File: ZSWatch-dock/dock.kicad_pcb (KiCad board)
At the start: 2 copper layers, 55.1 x 32.5 mm, 22 parts, among them IC1 STM32F072CBT6, IC2 TCR3UF20A,LM_CT, IC3 TXB0104QPWRQ1, IC4 XC9265C181MR-G, J1 USB4105-GF-A, J2 8.06.16, J3 Charger and programming heade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

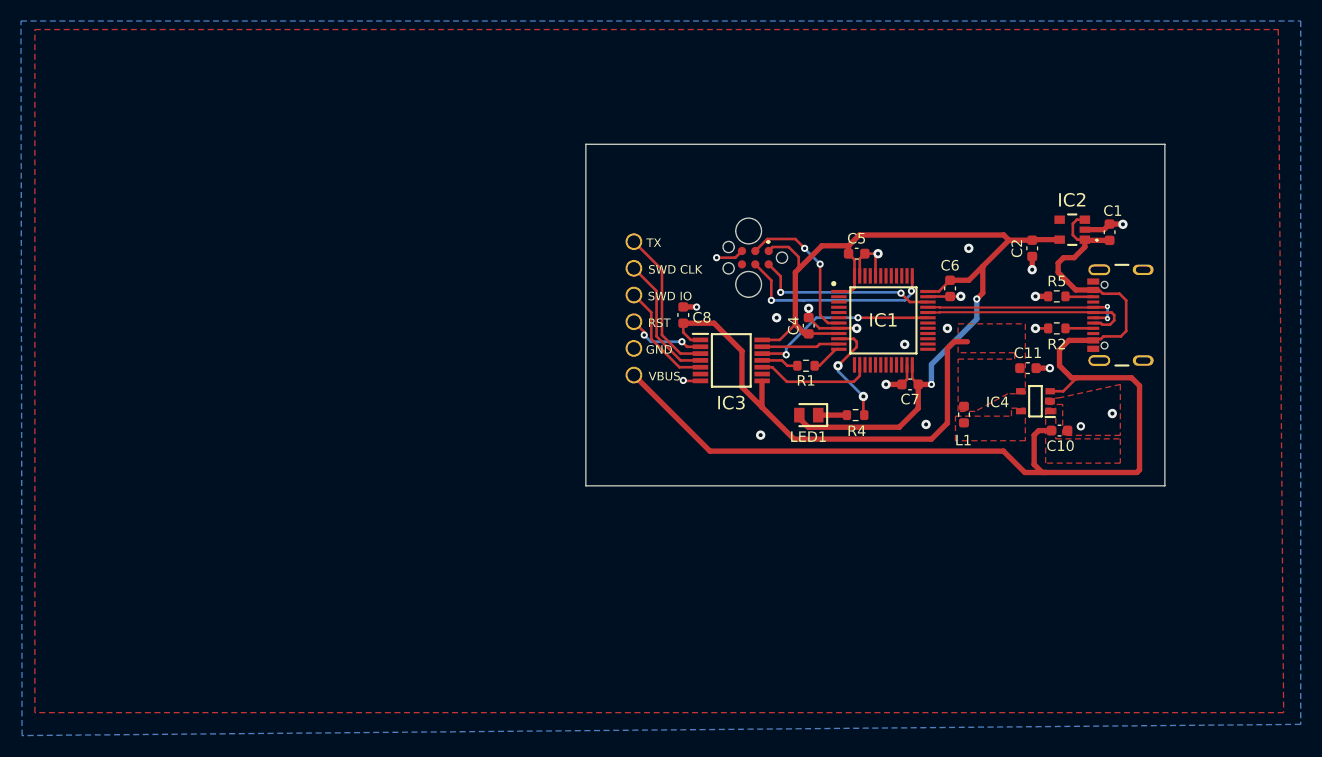
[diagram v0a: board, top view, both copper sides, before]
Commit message: Finished dock/debugger/programmer PCB.
Moved connectors around.
Added missing silkscreen.
Added extra connector for easy access to pins such as power etc.
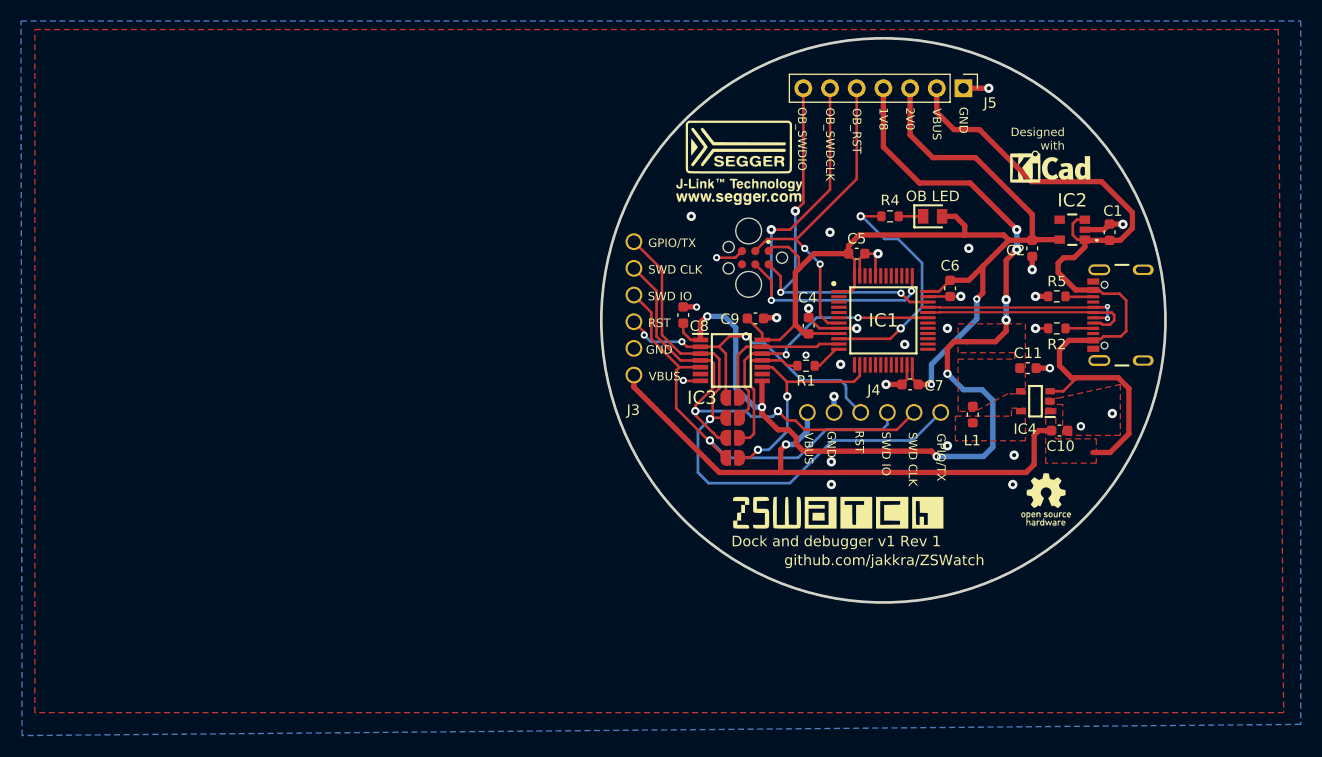
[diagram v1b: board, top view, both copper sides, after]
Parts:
- added C9: 0.1uF, Capacitor_SMD:C_0603_1608Metric, F.Cu at (140.7, 76.8)
- added G***: LOGO, LOGO, F.Cu at (168.9, 62.2)
- added G***: LOGO, LOGO, F.Cu at (148.6, 95.2)
- added G***: LOGO, LOGO, F.Cu at (168.4, 94.0)
- added G***: LOGO, LOGO, F.Cu at (139.2, 62.0)
- added J4: Charger and programming header (Placeholder), user_library:rtlecs-6-pin-2-54, F.Cu at (152.0, 85.7)
- added J5: Conn_01x07, Connector_PinHeader_2.54mm:PinHeader_1x07_P2.54mm_Vertical, F.Cu at (160.5, 54.9)
- added JP1: SolderJumper_2_Open, Jumper:SolderJumper-2_P1.3mm_Open_RoundedPad1.0x1.5mm, F.Cu at (138.6, 84.3)
- added JP2: SolderJumper_2_Open, Jumper:SolderJumper-2_P1.3mm_Open_RoundedPad1.0x1.5mm, F.Cu at (138.6, 88.1)
- added JP3: SolderJumper_2_Open, Jumper:SolderJumper-2_P1.3mm_Open_RoundedPad1.0x1.5mm, F.Cu at (138.6, 90.0)
- added JP4: SolderJumper_2_Open, Jumper:SolderJumper-2_P1.3mm_Open_RoundedPad1.0x1.5mm, F.Cu at (138.6, 86.2)
- OB LED: renamed from LED1
- moved OB LED 22.3 mm to (157.6, 67.1), turned to 0 degrees
- moved R4 19.2 mm to (153.5, 67.1), turned to 180 degrees
- moved L1 0.84 mm to (161.4, 85.9)
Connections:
- net Net-(IC3-Pad11) renamed /ZSWATCH_H_SWDCLK_PRE
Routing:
- net +1V8: track 46.9 -> 95.1 mm, vias 0 -> 8
- net /ZSWATCH_L_TX: track 14.4 -> 55.9 mm, vias 0 -> 1
- net /ZSWATCH_L_SWDCLK: track 12.5 -> 46.0 mm, vias 0 -> 2
- net /ZSWATCH_L_SWDIO: track 10.7 -> 41.5 mm, vias 0 -> 1
- net VBUS: track 107.6 -> 132.8 mm, vias 0 -> 1
- net /ZSWATCH_L_RESET: track 7.49 -> 31.9 mm, vias 2 -> 3
- net /OB_CLK: track 19.4 -> 42.9 mm, vias 2 -> 3
- net /OB_SWDIO: track 17.5 -> 37.9 mm, vias 2 -> 3
- net /OB_RESET: track 14.6 -> 31.5 mm
- net LED_OB: track 10.6 -> 23.0 mm
- net +2V0: track 91.9 -> 104.3 mm
- net /ZSWATCH_H_SWDIO: track 11.1 -> 21.5 mm, vias 0 -> 2
- net /ZSWATCH_H_SWDCLK_PRE: track 3.56 -> 13.2 mm
- net ZSWATCH_H_TX: track 17.7 -> 25.6 mm
- net /ZSWATCH_H_RESET: track 7.41 -> 14.2 mm
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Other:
- board size 55.1 x 32.5 mm -> 53.7 x 53.7 mm
- board text added: "1V8"
- board text added: "2V0"
- board text added: "Designed with"
- board text added: "Dock and debugger v1 Rev 1"
- board text added: "GPIO"
- board text added: "GPIO/TX"
- board text added: "OB_RST"
- board text added: "OB_SWDCLK"
- board text added: "OB_SWDIO"
- board text added: "github.com/jakkra/ZSWatch"
- board text removed: "TX"

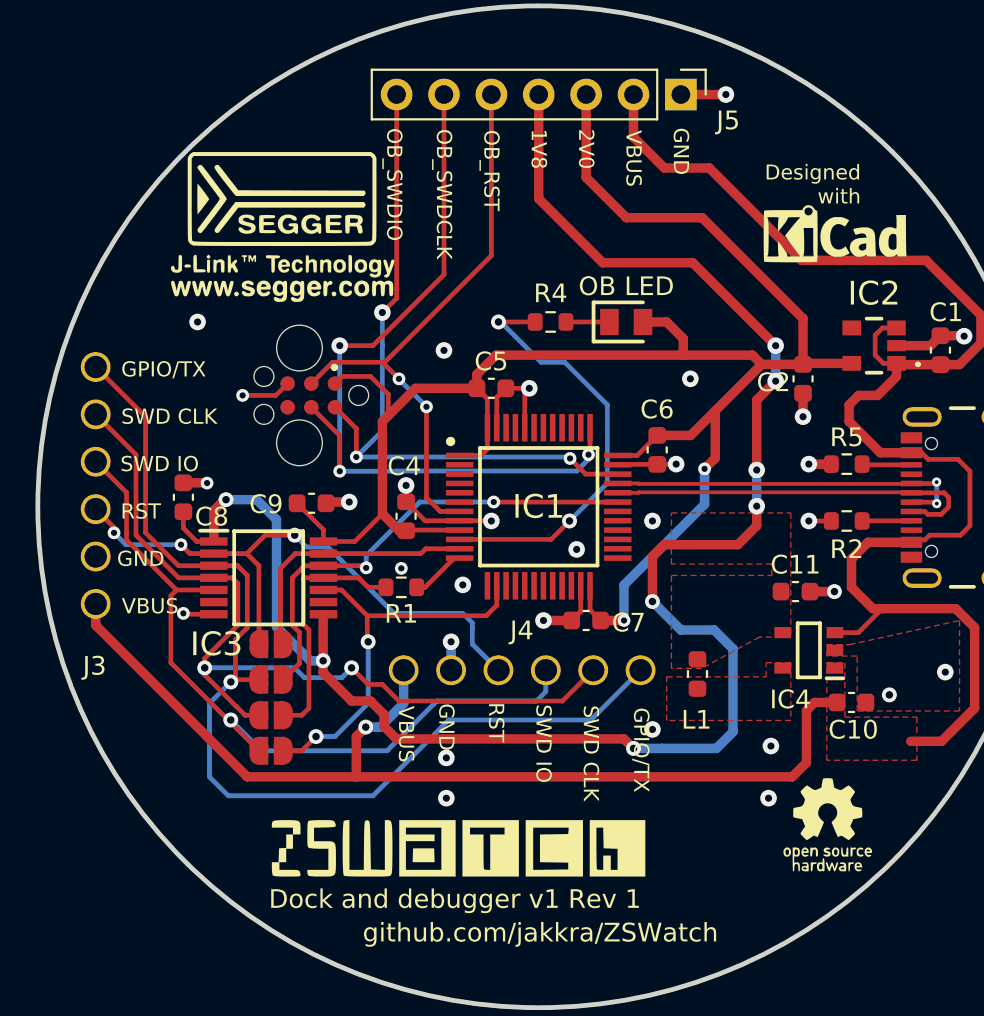
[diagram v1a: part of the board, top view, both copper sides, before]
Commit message: Dock PCB: Minor routing and silkscreen improvements.
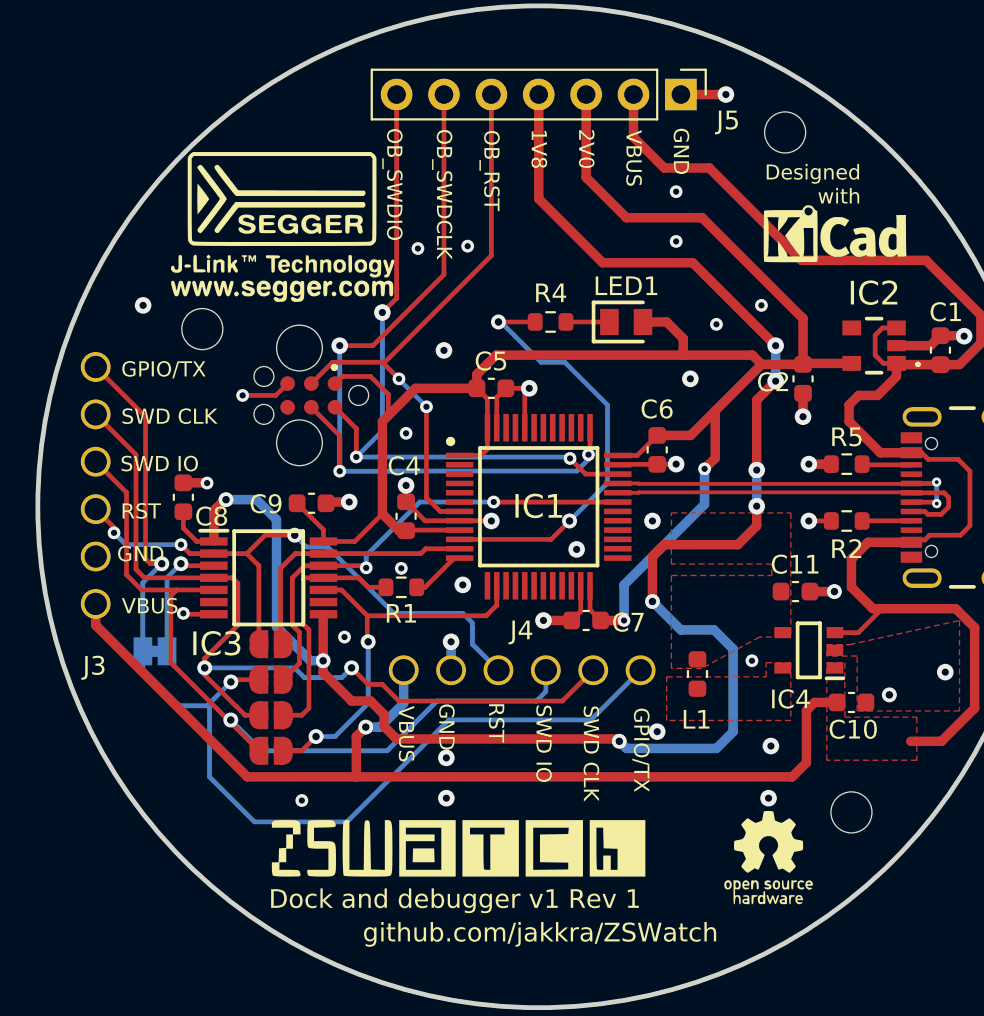
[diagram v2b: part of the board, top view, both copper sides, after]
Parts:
- added H1: MountingHole, MountingHole:MountingHole_2.2mm_M2, F.Cu at (169.7, 93.3)
- added H2: MountingHole, MountingHole:MountingHole_2.2mm_M2, F.Cu at (134.9, 67.4)
- added H3: MountingHole, MountingHole:MountingHole_2.2mm_M2, F.Cu at (166.1, 56.9)
- added J6: Conn_01x02, Jumper:SolderJumper-2_P1.3mm_Bridged_Pad1.0x1.5mm, B.Cu at (132.3, 84.7)
- J3: value Charger and programming header (Placeholder) -> Charger and programming headers
- J4: value Charger and programming header (Placeholder) -> Charger and programming header
- LED1: renamed from OB LED
- moved G*** 3.63 mm to (165.2, 95.8)
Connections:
- IC3 pad 3: /ZSWATCH_L_TX -> /L_TX
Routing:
- net /L_TX: track 0.00 -> 6.81 mm, vias 0 -> 1
- net /ZSWATCH_L_TX: track 55.9 -> 57.6 mm, vias 1 -> 2
- net /ZSWATCH_L_SWDIO: track 41.5 -> 42.6 mm
- net /ZSWATCH_L_SWDCLK: track 46.0 -> 47.1 mm
- net GND: vias 30 -> 40
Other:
- board text added: "Cut do disconnect ZSWatch IO/UART TX from VCOM"
- board text added: "Important: For use with ZSWatch only SEGGER OB Licence Required"
- board text removed: "GPIO"
